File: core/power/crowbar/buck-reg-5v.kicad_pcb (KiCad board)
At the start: 2 copper layers, 32 parts, among them P1 CONN_01X02, P2 CONN_01X02, U1 LM25576

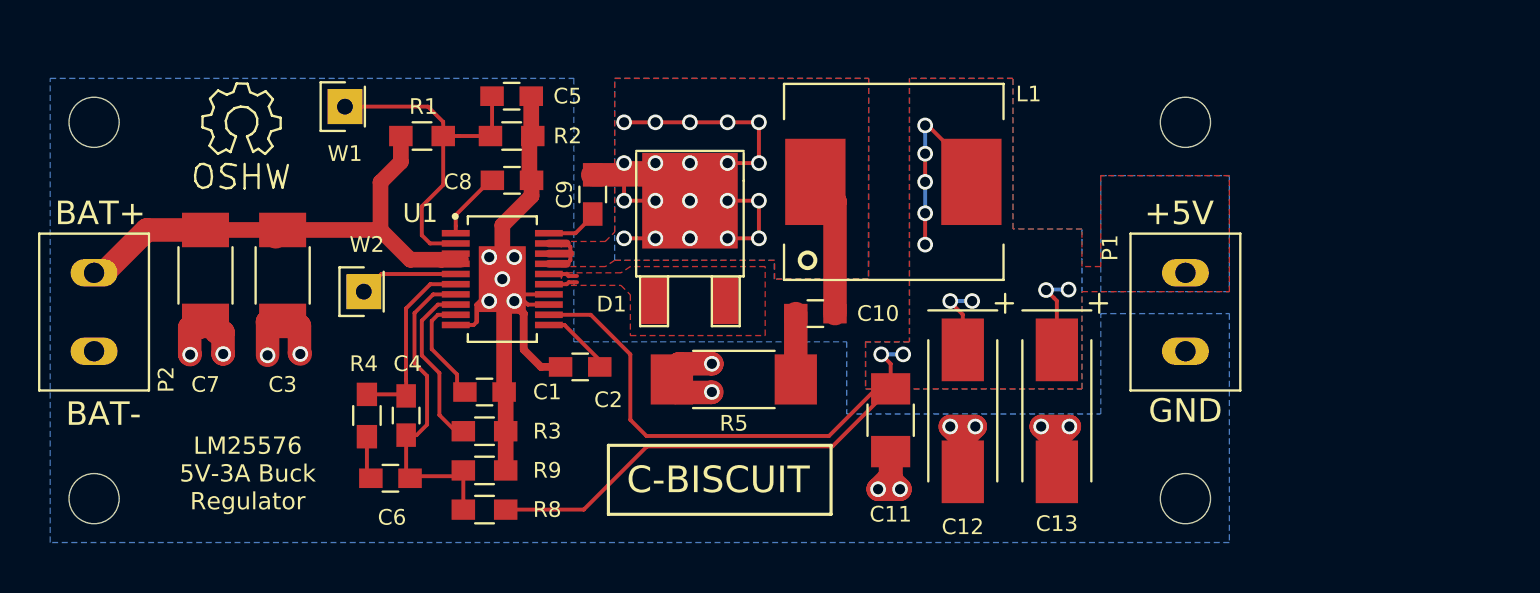
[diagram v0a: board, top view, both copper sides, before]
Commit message: Added mfg files. Still needs links to parts.
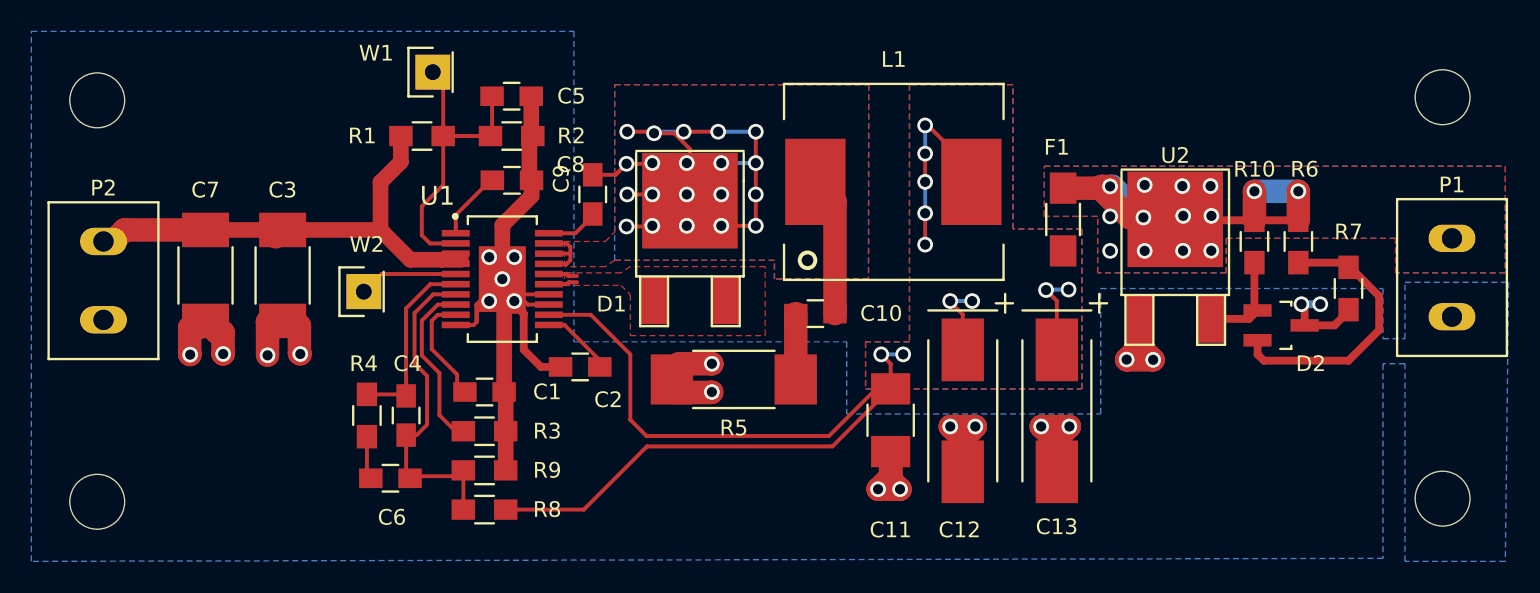
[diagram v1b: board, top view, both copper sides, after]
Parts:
- removed the REF** at (35.6, 89.8)
- removed the REF** at (35.6, 65.8)
- removed the REF** at (105.2, 89.8)
- removed the REF** at (105.2, 65.8)
- removed the REF** at (45.0, 65.8)
- added D2: LM431, TO_SOT_Packages_SMD:SOT-23_Handsoldering, F.Cu at (111.3, 78.8)
- added F1: 3A, Resistors_SMD:R_1206_HandSoldering, F.Cu at (97.4, 72.0)
- added R10: 220, Resistors_SMD:R_0805_HandSoldering, F.Cu at (109.6, 73.4)
- added R6: 3.48K, Resistors_SMD:R_0805_HandSoldering, F.Cu at (112.4, 73.4)
- added R7: 2.49K, Resistors_SMD:R_0805_HandSoldering, F.Cu at (115.6, 76.4)
- added REF**: MountingHole_3mm, Mounting_Holes:MountingHole_3mm, F.Cu at (35.8, 64.4)
- added REF**: MountingHole_3mm, Mounting_Holes:MountingHole_3mm, F.Cu at (35.8, 90.0)
- added REF**: MountingHole_3mm, Mounting_Holes:MountingHole_3mm, F.Cu at (121.6, 89.8)
- added REF**: MountingHole_3mm, Mounting_Holes:MountingHole_3mm, F.Cu at (121.6, 64.2)
- added U2: BT151S-500R, TO_SOT_Packages_SMD:TO-252-2Lead, F.Cu at (104.6, 78.3)
- moved P1 17.1 mm to (122.2, 73.2)
- moved W1 6.02 mm to (57.2, 62.6)
- moved P2 2.09 mm to (36.2, 73.4)
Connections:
- C11 pad 1: +5V -> /OUT
- C12 pad 1: +5V -> /OUT
- C13 pad 1: +5V -> /OUT
- L1 pad 2: +5V -> /OUT
- R8 pad 1: +5V -> /OUT
- U1 pad 12: +5V -> /OUT
- U1 pad EP: (no net) -> GND
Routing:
- net /OUT: track 0.00 -> 84.6 mm, vias 0 -> 11
- net +5V: track 84.6 -> 23.5 mm, vias 11 -> 12
- net Net-(D2-Pad2): track 0.00 -> 17.8 mm
- net GND: track 92.0 -> 105.7 mm, vias 17 -> 21
- net Net-(D2-Pad1): track 0.00 -> 6.32 mm
- net /SD: track 22.4 -> 19.2 mm
- net /BAT_IN: track 33.8 -> 32.4 mm
- net /SW: track 64.2 -> 64.8 mm
- net (no net): vias 0 -> 2
- added copper zone on B.Cu, net /OUT
- added copper zone on F.Cu, net /OUT
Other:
- board text removed: "+5V"
- board text removed: "BAT+"
- board text removed: "BAT-"
- board text removed: "C-BISCUIT"
- board text removed: "GND"
- board text removed: "LM25576 5V-3A Buck Regulator"
